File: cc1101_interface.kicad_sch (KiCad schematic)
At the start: 2 parts, among them J3 CONN_CC1101_LARGE, J4 CONN_CC1101_SMALL

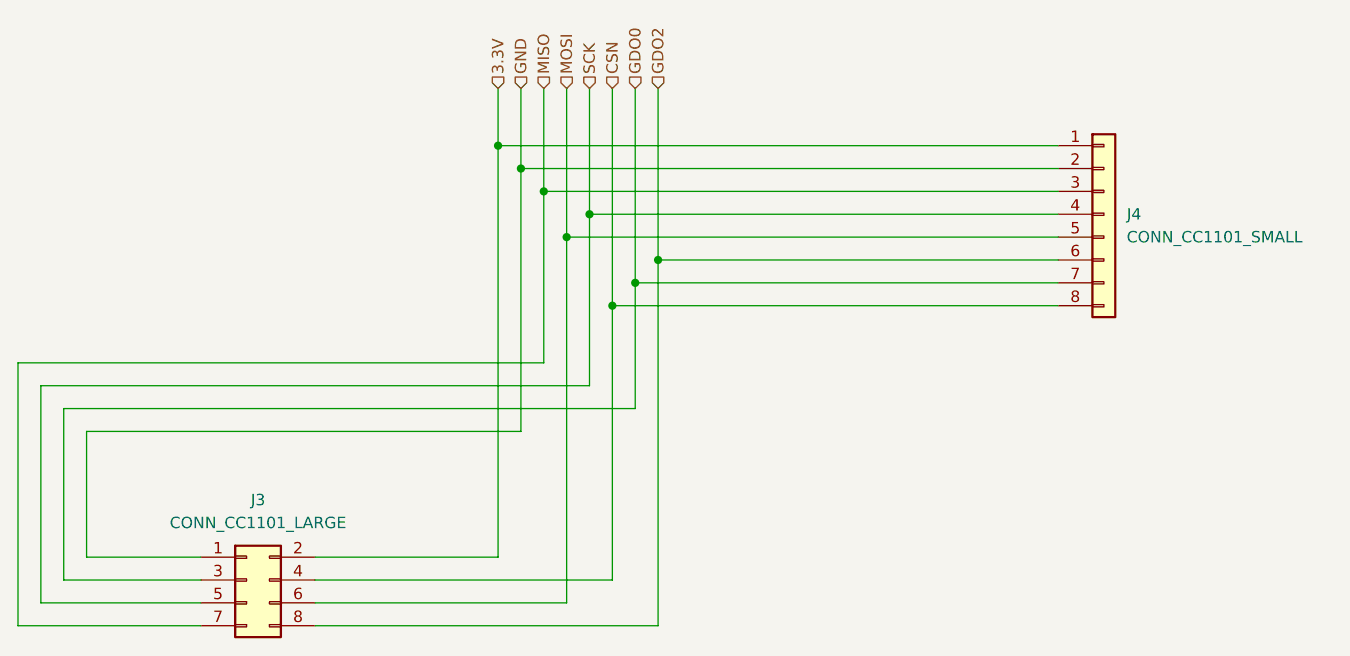
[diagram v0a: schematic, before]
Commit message: Re-labelled all parts.
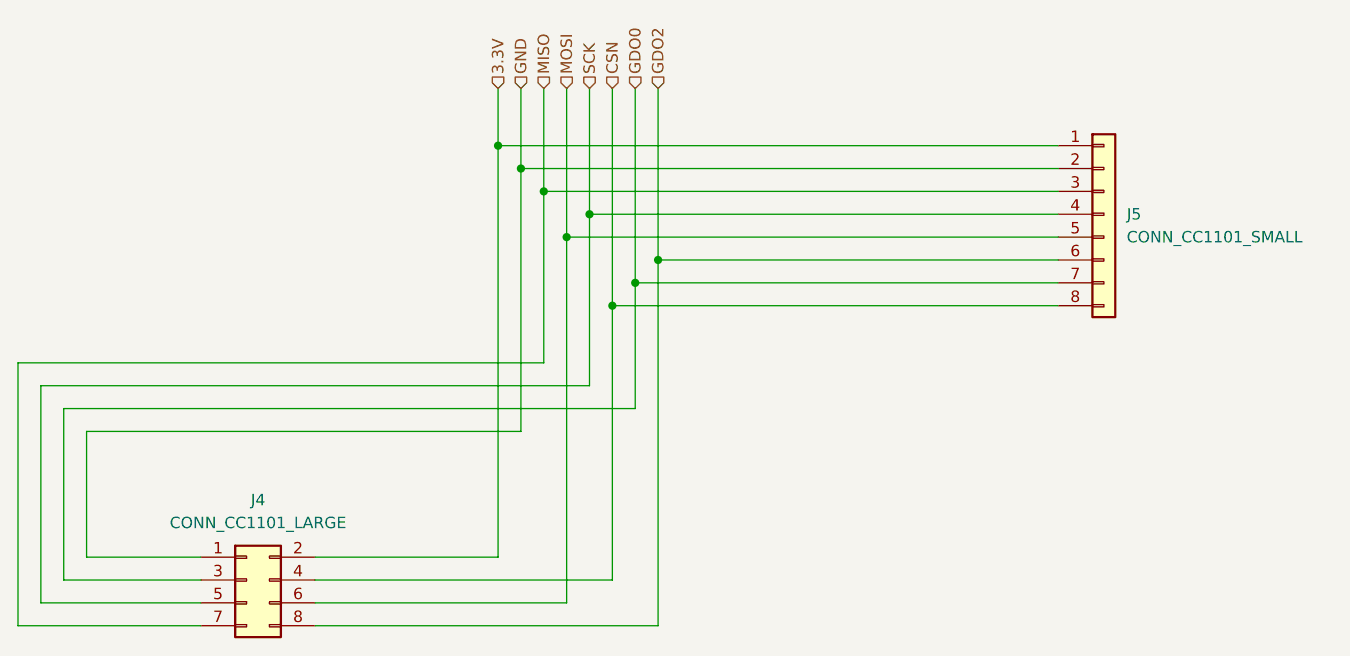
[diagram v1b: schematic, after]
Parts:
- renumbered J3 to J4, J4 to J5
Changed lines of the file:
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@@
 		(dnp no)
 		(fields_autoplaced yes)
-		(property "Reference" "J4"
+		(property "Reference" "J5"
 			(at 179.07 77.4699 0)
 			(effects
@@
 			(project ""
 				(path "/64404f27-cfd6-41d9-8edb-810ebab8cc14/68a209f5-f150-4b46-8b9b-45a7916aa769"
-					(reference "J4")
+					(reference "J5")
 					(unit 1)
 				)
@@
 		(dnp no)
 		(fields_autoplaced yes)
-		(property "Reference" "J3"
+		(property "Reference" "J4"
 			(at 82.55 109.22 0)
 			(effects
@@
 			(project ""
 				(path "/64404f27-cfd6-41d9-8edb-810ebab8cc14/68a209f5-f150-4b46-8b9b-45a7916aa769"
-					(reference "J3")
+					(reference "J4")
 					(unit 1)
 				)
